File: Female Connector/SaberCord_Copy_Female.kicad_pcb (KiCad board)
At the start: 2 copper layers, 30 x 20.3 mm, 5 parts, among them J1 Conn_02x07_Row_Letter_Last, J2 Conn_02x12_Row_Letter_Last

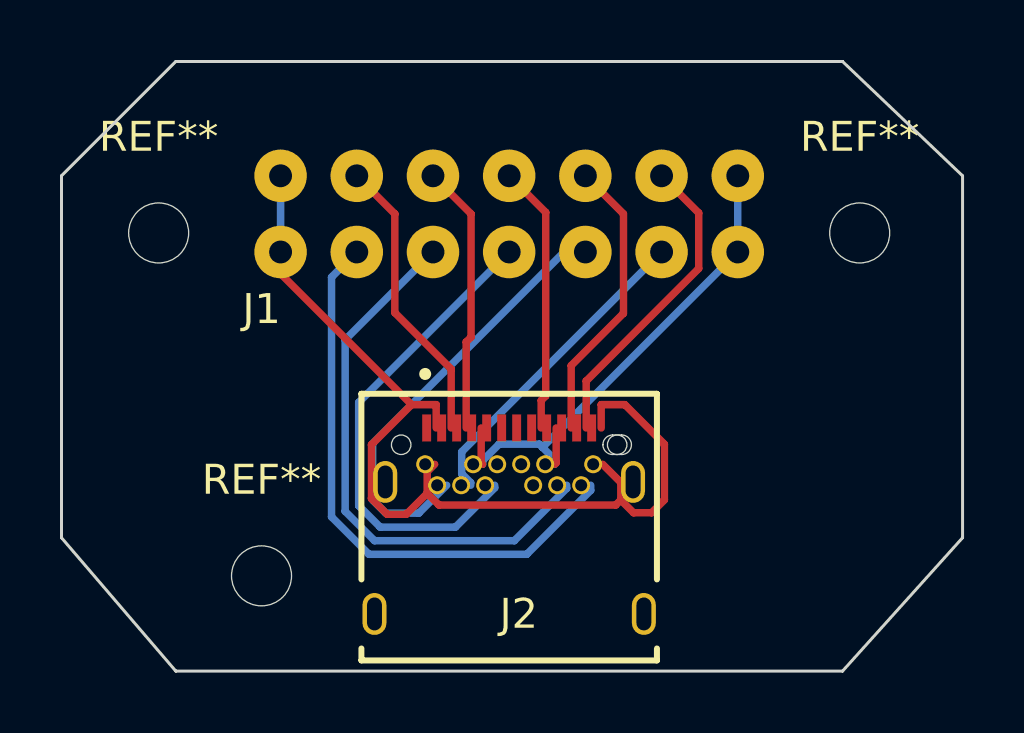
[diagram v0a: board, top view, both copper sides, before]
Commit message: fusion360 possible, additional files added
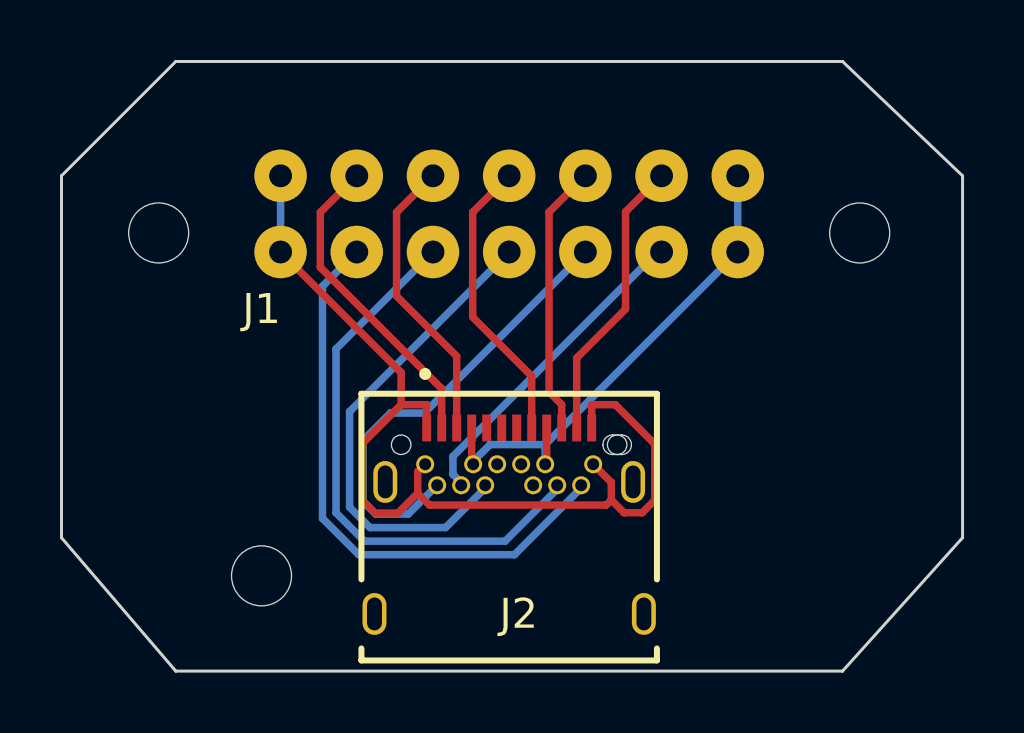
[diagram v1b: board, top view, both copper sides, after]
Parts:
- renumbered REF** to bottomleft, REF** to topleft, REF** to toprighjt
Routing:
- net /CAN1_H: track 10.5 -> 9.58 mm
- net /CAN0_H: track 9.71 -> 10.6 mm
- net /SBU1: track 8.97 -> 9.72 mm
- net /CAN0_L: track 9.00 -> 9.74 mm
- net /CAN1_L: track 9.65 -> 9.08 mm

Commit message: fixed female connector mirror
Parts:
- added toprighjt: MountingHole_2mm, MountingHole:MountingHole_2mm, F.Cu at (148.8, 93.0)
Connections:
- J1 pad 10: /CAN2_L -> /CAN0_L
- J1 pad 11: /SBU2 -> /SBU1
- J1 pad 12: /CAN3_H -> /CAN1_L
- J1 pad 13: /CAN3_L -> /CAN1_H
- J1 pad 2: /CAN0_H -> /CAN2_H
- J1 pad 3: /CAN0_L -> /CAN2_L
- J1 pad 4: /SBU1 -> /SBU2
- J1 pad 5: /CAN1_L -> /CAN3_H
- J1 pad 6: /CAN1_H -> /CAN3_L
- J1 pad 9: /CAN2_H -> /CAN0_H
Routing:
- net /GND: track 33.2 -> 21.0 mm
- net /SBU1: track 9.72 -> 6.18 mm
- net /CAN0_L: track 9.74 -> 6.19 mm
- net /CAN0_H: track 10.6 -> 7.04 mm
- net /CAN1_L: track 9.08 -> 6.19 mm
- net /CAN3_H: track 15.1 -> 12.4 mm
- net /CAN1_H: track 9.58 -> 7.04 mm
- net /CAN3_L: track 10.9 -> 13.2 mm
- net /CAN2_H: track 19.5 -> 20.7 mm
- net /SBU2: track 16.1 -> 17.2 mm
- net /CAN2_L: track 18.6 -> 19.5 mm
